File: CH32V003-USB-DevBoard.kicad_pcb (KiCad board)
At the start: 2 copper layers, 15.8 x 26.1 mm, 23 parts, among them J1 USB_C_Receptacle_USB2.0, J2 Conn_01x10, J3 Conn_01x10, J4 Conn_01x01, SW1 SW_Push, U1 ME6211A33M3G-N, U3 CH32V003F4U6, Y1 24MHz

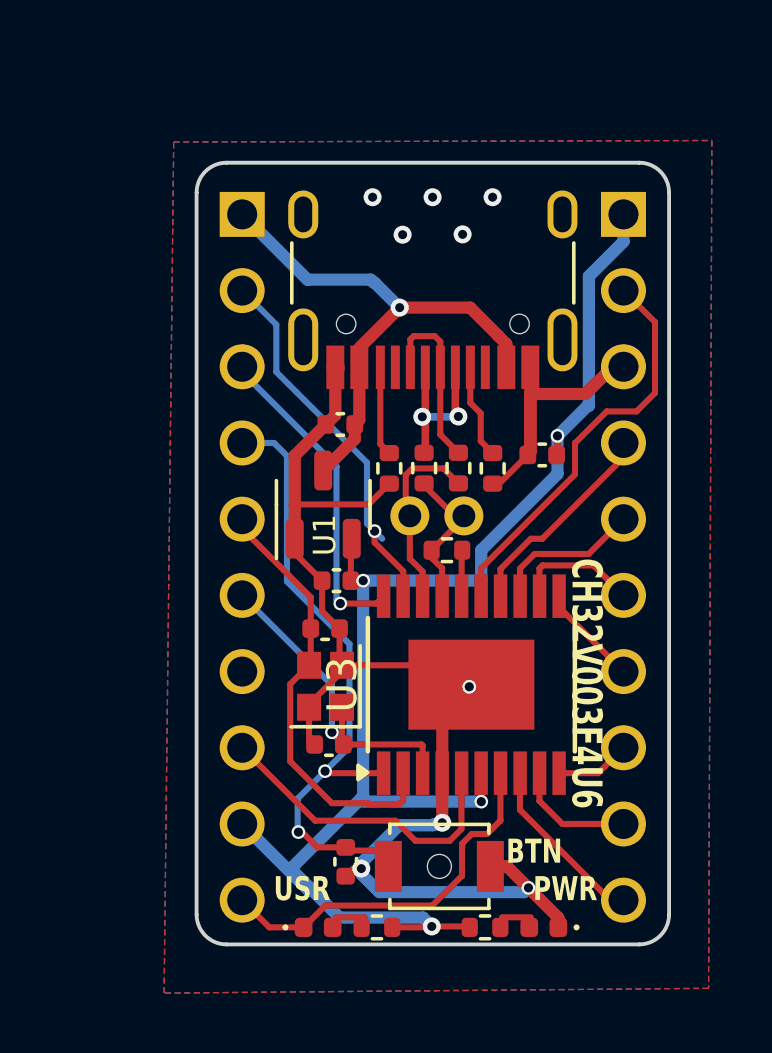
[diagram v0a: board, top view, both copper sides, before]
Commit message: Make design easier to hand solder Switch to ch340n instead of S/W bit banged USB
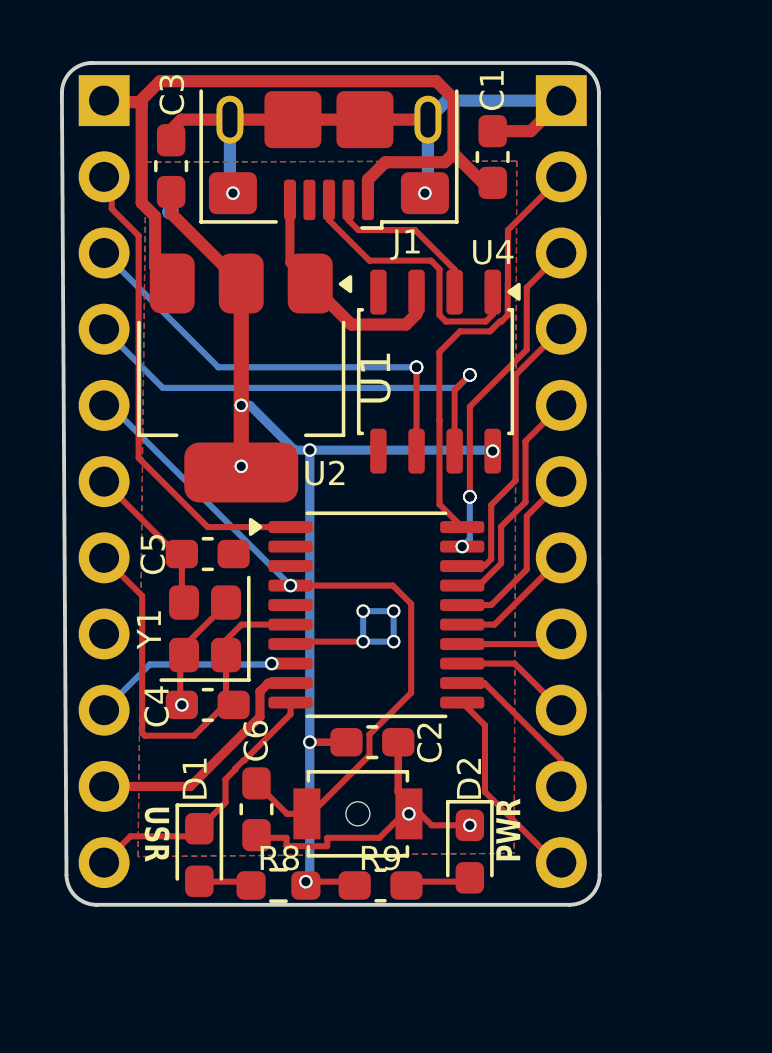
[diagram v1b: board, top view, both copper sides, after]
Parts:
- removed J4: Conn_01x01, Library:TestPoint_01x02
- removed R1: 1k5, Resistor_SMD:R_0402_1005Metric
- removed R2, R3: 5k1, Resistor_SMD:R_0402_1005Metric
- removed R4, R5: 33R, Resistor_SMD:R_0402_1005Metric
- removed U3: CH32V003F4U6, Package_SO:ETSSOP-20-1EP_4.4x6.5mm_P0.65mm_EP3x4.2mm
- added U2: CH32V003FxPx, Package_SO:TSSOP-20_4.4x6.5mm_P0.65mm, F.Cu at (147.2, 105.2)
- added U4: CH340N, Package_SO:JEITA_SOIC-8_3.9x4.9mm_P1.27mm, F.Cu at (149.1, 97.1)
- C1, C2, C3, C4, C5, C6: footprint Capacitor_SMD:C_0402_1005Metric -> Capacitor_SMD:C_0603_1608Metric_Pad1.08x0.95mm_HandSolder
- D1, D2: footprint LED_SMD:LED_0402_1005Metric -> LED_SMD:LED_0603_1608Metric_Pad1.05x0.95mm_HandSolder
- J1: value USB_C_Receptacle_USB2.0 -> USB_B_Micro; footprint Connector_USB:USB_C_Receptacle_HRO_TYPE-C-31-M-12 -> Connector_USB:USB_Micro-B_Amphenol_10118193-0001LF_Horizontal
- J2, J3: value Conn_01x10 -> Conn_01x11_Pin; footprint Library:PinHeader_1x10_Small -> Connector_PinHeader_2.54mm:PinHeader_1x11_P2.54mm_Vertical
- R8: footprint Resistor_SMD:R_0402_1005Metric -> Resistor_SMD:R_0603_1608Metric_Pad0.98x0.95mm_HandSolder
- R9: footprint Resistor_SMD:R_0402_1005Metric -> Capacitor_SMD:C_0603_1608Metric_Pad1.08x0.95mm_HandSolder
- U1: value ME6211A33M3G-N -> AMS1117-3.3; footprint Package_TO_SOT_SMD:SOT-23-3 -> Package_TO_SOT_SMD:SOT-223-3_TabPin2
- Y1: footprint Crystal:Crystal_SMD_2016-4Pin_2.0x1.6mm -> Crystal:Crystal_SMD_2520-4Pin_2.5x2.0mm
- moved C3 15.7 mm to (140.3, 90.3), turned to 90 degrees
- moved C1 10.3 mm to (151.1, 90.0), turned to 90 degrees
- moved J2 5.96 mm to (138.1, 88.1)
- moved C2 5.52 mm to (147.0, 109.5), turned to 0 degrees
- moved J1 5.45 mm to (145.6, 88.7)
- moved U1 5.03 mm to (142.7, 97.3), turned to -90 degrees
- moved D1 4.64 mm to (141.3, 113.2), turned to -90 degrees
- moved C5 4.64 mm to (141.6, 103.2)
- moved Y1 4.45 mm to (141.5, 105.7)
- moved J3 4.32 mm to (153.3, 88.1)
- moved C4 4.25 mm to (141.6, 108.2)
- moved R9 3.75 mm to (147.3, 114.3)
- moved R8 3.57 mm to (143.9, 114.3)
- moved D2 3.53 mm to (150.3, 113.1), turned to -90 degrees
- moved C6 3.45 mm to (143.2, 111.7)
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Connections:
- C1 pad 1: VBUS -> +5V
- C2 pad 1: +3V3 -> +3.3V
- C3 pad 1: +3V3 -> +3.3V
- J2 pad 1: VBUS -> +5V
- J2 pad 10: PC0 -> +3V3
- J2 pad 2: PD5 -> PD4
- J2 pad 3: PD6 -> URX
- J2 pad 4: PD7 -> UTX
- J2 pad 5: PA1 -> PD7
- J2 pad 6: PA2 -> PA1
- J2 pad 7: GND -> PA2
- J2 pad 8: PD0 -> GND
- J2 pad 9: +3V3 -> PD0
- J3 pad 1: +3V3 -> GND
- J3 pad 10: PC1 -> PC2
- J3 pad 2: SWIO -> PD3
- J3 pad 3: GND -> PD2
- J3 pad 4: PC7 -> SWIO
- J3 pad 5: PC6 -> PC7
- J3 pad 6: PC5 -> PC6
- J3 pad 7: PC4 -> PC5
- J3 pad 8: PC3 -> PC4
- J3 pad 9: PC2 -> PC3
- R8 pad 1: +3V3 -> +3.3V
- R9 pad 1: +3V3 -> +3.3V
- U1 pad 2: +3V3 -> +3.3V
- U1 pad 3: VBUS -> +5V
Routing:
- net +3V3: track 47.5 -> 8.13 mm, vias 4 -> 0
- net +3.3V: track 0.00 -> 36.9 mm, vias 0 -> 6
- net +5V: track 0.00 -> 26.5 mm
- net VBUS: track 17.2 -> 0.00 mm, vias 1 -> 0
- net UTX: track 0.00 -> 15.9 mm, vias 0 -> 2
- net PD4: track 0.00 -> 15.9 mm
- net URX: track 0.00 -> 14.8 mm, vias 0 -> 2
- net PD3: track 0.00 -> 14.3 mm
- net PD5: track 12.8 -> 0.00 mm, vias 1 -> 0
- net PD2: track 0.00 -> 11.2 mm, vias 0 -> 3
- net PD6: track 10.8 -> 0.00 mm, vias 1 -> 0
- net PA1: track 14.7 -> 5.11 mm
- net Net-(J1-D+): track 0.00 -> 9.28 mm
- net USB_DP: track 6.46 -> 0.00 mm
- net /D+: track 6.00 -> 0.00 mm
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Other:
- board size 15.8 x 26.1 mm -> 17.9 x 28.1 mm
- board text added: "D1/SWIO"
- board text added: "D2"
- board text added: "D3"
- board text added: "D4"
- board text added: "PA1"
- board text added: "PA2"
- board text added: "RX/D5"
- board text added: "Rev. 1.0"
- board text added: "TX/D6"
- board text removed: "A1"
- board text removed: "A2"
- board text removed: "BTN"
- board text removed: "CH32V003F4U6"
- board text removed: "D5"
- board text removed: "D6"
- board text removed: "Rev. 1"
- board text removed: "SWIO"

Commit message: Update img/front-and-back/side.png Update README.md text
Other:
- board text added: "CH32V003 DevBoard"
- board text removed: "CH32V003 USB DevBoard"
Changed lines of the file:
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@@
 		)
 	)
-	(gr_text "CH32V003\nUSB DevBoard\n"
+	(gr_text "CH32V003\nDevBoard\n"
 		(at 146.736 103.34 90)
 		(layer "B.SilkS")
@@
 	)
 	(segment
+		(start 138.1 88.1)
+		(end 138.1 88.5064)
+		(width 0.4064)
+		(layer "F.Cu")
+		(net "+5V")
+	)
+	(segment
+		(start 138.1508 88.1508)
+		(end 138.1 88.1)
+		(width 0.4064)
+		(layer "F.Cu")
+		(net "+5V")
+	)
+	(segment
+		(start 149.4564 90.1548)
+		(end 149.7482 89.863)
+		(width 0.4064)
+		(layer "F.Cu")
+		(net "+5V")
+	)
+	(segment
+		(start 146.895 90.735001)
+		(end 147.475201 90.1548)
+		(width 0.4064)
+		(layer "F.Cu")
+		(net "+5V")
+	)
+	(segment
+		(start 149.171407 87.4548)
+		(end 139.9644 87.4548)
+		(width 0.4064)
+		(layer "F.Cu")
+		(net "+5V")
+	)
+	(segment
+		(start 147.475201 90.1548)
+		(end 149.4564 90.1548)
+		(width 0.4064)
+		(layer "F.Cu")
+		(net "+5V")
+	)
+	(segment
+		(start 139.801799 93.625799)
+		(end 139.801799 91.960429)
+		(width 0.4064)
+		(layer "F.Cu")
+		(net "+5V")
+	)
+	(segment
+		(start 150.7284 90.8432)
+		(end 149.7482 89.863)
+		(width 0.4064)
+		(layer "F.Cu")
+		(net "+5V")
+	)
+	(segment
+		(start 149.7482 89.863)
+		(end 149.7482 88.031593)
+		(width 0.4064)
+		(layer "F.Cu")
+		(net "+5V")
+	)
+	(segment
+		(start 139.3532 88.2356)
+		(end 139.2684 88.1508)
+		(width 0.4064)
+		(layer "F.Cu")
+		(net "+5V")
+	)
+	(segment
+		(start 149.7482 88.031593)
+		(end 149.171407 87.4548)
+		(width 0.4064)
+		(layer "F.Cu")
+		(net "+5V")
+	)
+	(segment
+		(start 151.054 90.8432)
+		(end 150.7284 90.8432)
+		(width 0.4064)
+		(layer "F.Cu")
+		(net "+5V")
+	)
+	(segment
+		(start 139.9644 87.4548)
+		(end 139.2684 88.1508)
+		(width 0.4064)
+		(layer "F.Cu")
+		(net "+5V")
+	)
+	(segment
+		(start 139.801799 91.960429)
+		(end 139.3532 91.51183)
+		(width 0.4064)
+		(layer "F.Cu")
+		(net "+5V")
+	)
+	(segment
+		(start 139.2684 88.1508)
+		(end 138.1508 88.1508)
+		(width 0.4064)
+		(layer "F.Cu")
+		(net "+5V")
+	)
+	(segment
+		(start 146.895 91.41)
+		(end 146.895 90.735001)
+		(width 0.4064)
+		(layer "F.Cu")
+		(net "+5V")
+	)
+	(segment
+		(start 139.3532 91.51183)
+		(end 139.3532 88.2356)
+		(width 0.4064)
+		(layer "F.Cu")
+		(net "+5V")
+	)
+	(segment
+		(start 140.372 94.196)
+		(end 139.801799 93.625799)
+		(width 0.4064)
+		(layer "F.Cu")
+		(net "+5V")
+	)
+	(segment
 		(start 148.178 114.135)
 		(end 150.165 114.135)
@@
 	)
 	(segment
-		(start 138.1 88.1)
-		(end 138.1 88.5064)
-		(width 0.4064)
-		(layer "F.Cu")
-		(net "+5V")
-	)
-	(segment
-		(start 138.1508 88.1508)
-		(end 138.1 88.1)
-		(width 0.4064)
-		(layer "F.Cu")
-		(net "+5V")
-	)
-	(segment
-		(start 149.4564 90.1548)
-		(end 149.7482 89.863)
-		(width 0.4064)
-		(layer "F.Cu")
-		(net "+5V")
-	)
-	(segment
-		(start 146.895 90.735001)
-		(end 147.475201 90.1548)
-		(width 0.4064)
-		(layer "F.Cu")
-		(net "+5V")
-	)
-	(segment
-		(start 149.171407 87.4548)
-		(end 139.9644 87.4548)
-		(width 0.4064)
-		(layer "F.Cu")
-		(net "+5V")
-	)
-	(segment
-		(start 147.475201 90.1548)
-		(end 149.4564 90.1548)
-		(width 0.4064)
-		(layer "F.Cu")
-		(net "+5V")
-	)
-	(segment
-		(start 139.801799 93.625799)
-		(end 139.801799 91.960429)
-		(width 0.4064)
-		(layer "F.Cu")
-		(net "+5V")
-	)
-	(segment
-		(start 150.7284 90.8432)
-		(end 149.7482 89.863)
-		(width 0.4064)
-		(layer "F.Cu")
-		(net "+5V")
-	)
-	(segment
-		(start 149.7482 89.863)
-		(end 149.7482 88.031593)
-		(width 0.4064)
-		(layer "F.Cu")
-		(net "+5V")
-	)
-	(segment
-		(start 139.3532 88.2356)
-		(end 139.2684 88.1508)
-		(width 0.4064)
-		(layer "F.Cu")
-		(net "+5V")
-	)
-	(segment
-		(start 149.7482 88.031593)
-		(end 149.171407 87.4548)
-		(width 0.4064)
-		(layer "F.Cu")
-		(net "+5V")
-	)
-	(segment
-		(start 151.054 90.8432)
-		(end 150.7284 90.8432)
-		(width 0.4064)
-		(layer "F.Cu")
-		(net "+5V")
-	)
-	(segment
-		(start 139.9644 87.4548)
-		(end 139.2684 88.1508)
-		(width 0.4064)
-		(layer "F.Cu")
-		(net "+5V")
-	)
-	(segment
-		(start 139.801799 91.960429)
-		(end 139.3532 91.51183)
-		(width 0.4064)
-		(layer "F.Cu")
-		(net "+5V")
-	)
-	(segment
-		(start 139.2684 88.1508)
-		(end 138.1508 88.1508)
-		(width 0.4064)
-		(layer "F.Cu")
-		(net "+5V")
-	)
-	(segment
-		(start 146.895 91.41)
-		(end 146.895 90.735001)
-		(width 0.4064)
-		(layer "F.Cu")
-		(net "+5V")
-	)
-	(segment
-		(start 139.3532 91.51183)
-		(end 139.3532 88.2356)
-		(width 0.4064)
-		(layer "F.Cu")
-		(net "+5V")
-	)
-	(segment
-		(start 140.372 94.196)
-		(end 139.801799 93.625799)
-		(width 0.4064)
-		(layer "F.Cu")
-		(net "+5V")
-	)
-	(segment

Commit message: Run Design Rule Check & fix errors Generate gerbers
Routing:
- net GND: track 51.9 -> 84.0 mm, vias 9 -> 12
- net UTX: track 15.9 -> 22.9 mm, vias 2 -> 3
- net URX: track 14.8 -> 20.7 mm
- net PA1: track 5.11 -> 9.34 mm, vias 0 -> 2
- net +3.3V: track 36.9 -> 36.8 mm, vias 6 -> 7
